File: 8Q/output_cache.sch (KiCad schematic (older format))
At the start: 21 parts

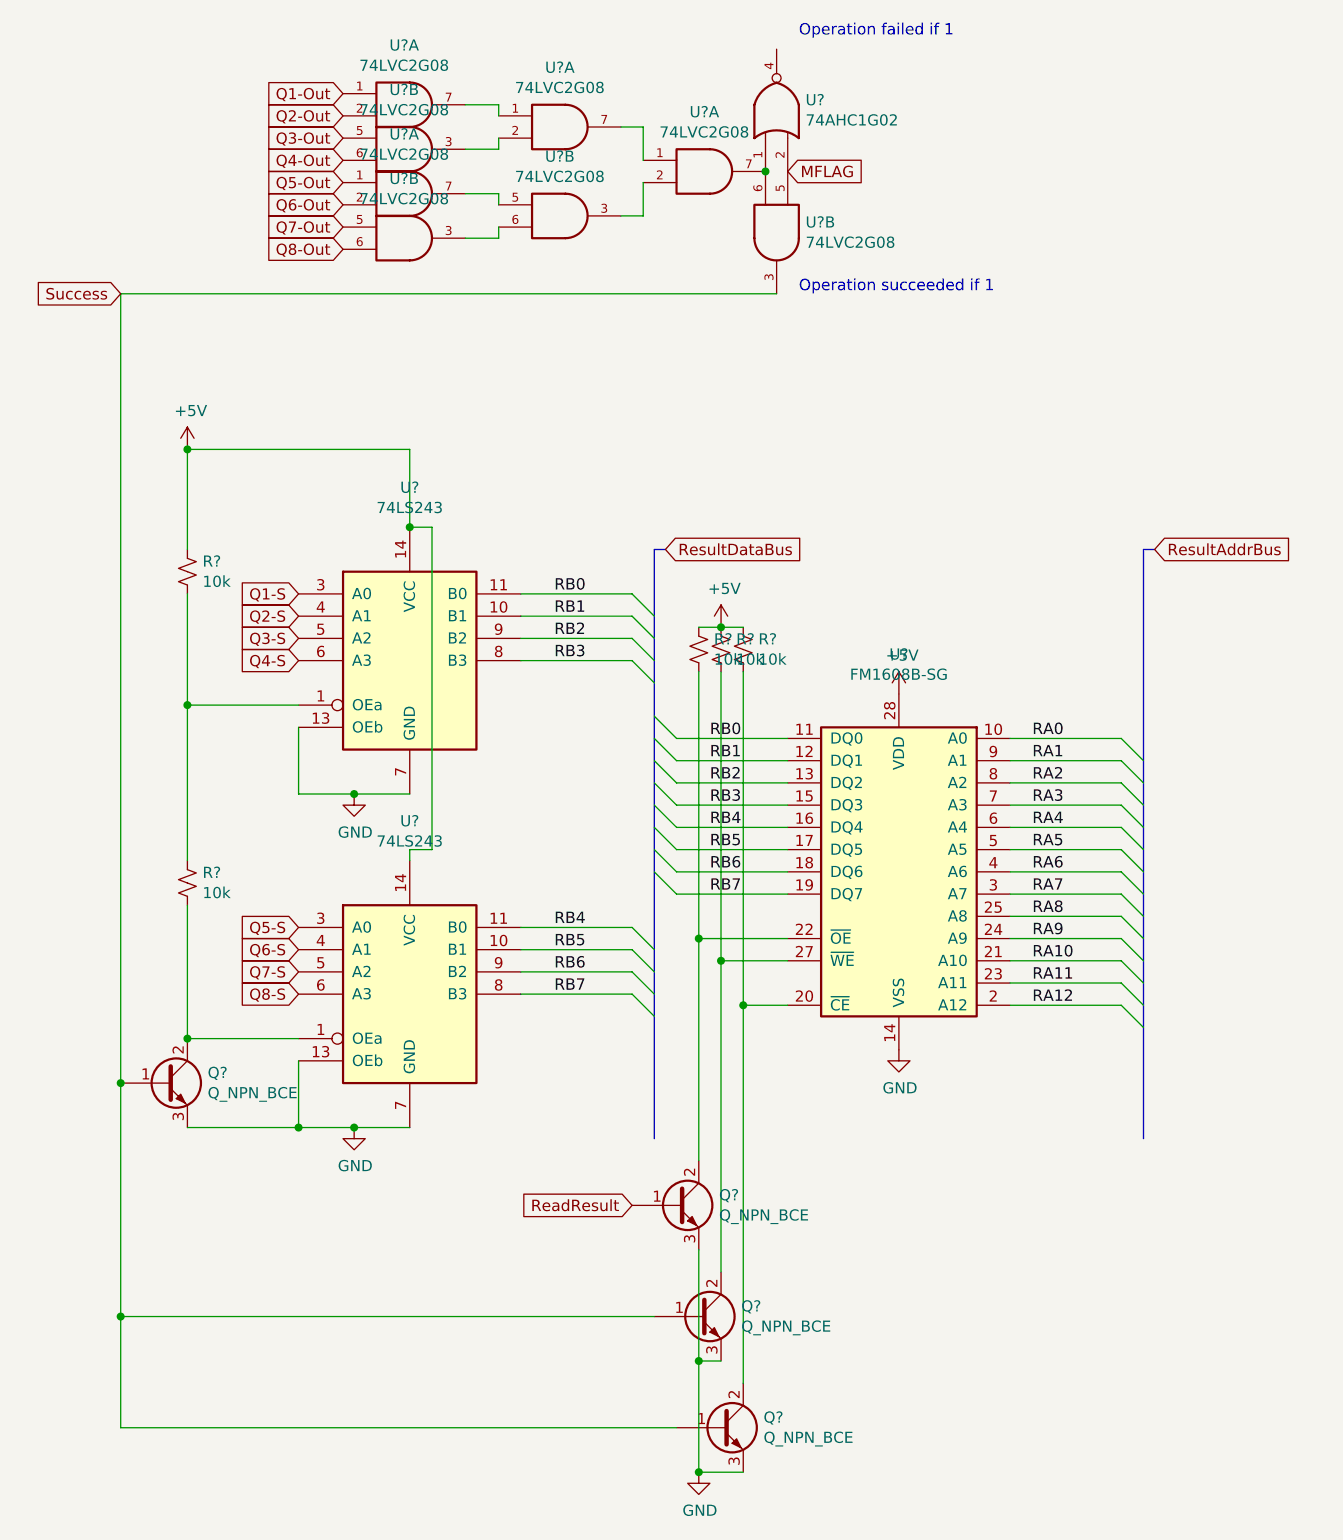
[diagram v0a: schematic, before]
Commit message: modified:   8Q/8Q-cache.lib 	new file:   8Q/8Q-rescue.dcm 	new file:   8Q/8Q-rescue.lib 	modified:   8Q/8Q.kicad_pcb 	modified:   8Q/8Q.sch 	modified:   8Q/8_qp_io.sch 	new file:   8Q/QGates.pretty/CH-Gate.kicad_mod 	new file:   8Q/QGates.pretty/CX-Gate.kicad_mod 	new file:   8Q/QGates.pretty/CY-Gate.kicad_mod 	new file:   8Q/QGates.pretty/CZ-Gate.kicad_mod 	new file:   8Q/QGates.pretty/H-Gate.kicad_mod 	new file:   8Q/QGates.pretty/Measure.kicad_mod 	new file:   8Q/QGates.pretty/Photon-Source.kicad_mod 	new file:   8Q/QGates.pretty/X-Gate.kicad_mod 	new file:   8Q/QGates.pretty/Y-Gate.kicad_mod 	new file:   8Q/QGates.pretty/Z-Gate.kicad_mod 	modified:   8Q/control_logic.sch 	modified:   8Q/cpu.sch 	modified:   8Q/inorder.sch 	modified:   8Q/instruction_bus.sch 	modified:   8Q/output_cache.sch 	modified:   8Q/power.sch 	modified:   8Q/preprocessor.sch 	modified:   8Q/qpower.sch 	modified:   8Q/qpu.sch 	new file:   8Q/sym-lib-table Introduced embedded QSeven module to replace CPU Computer now has support for: * 10Gbps Ethernet * 1xUSB3.0 * 4xUSB2.0 * 1xJTAG * 1xCAN * 1-Wire Bus * 1xSMBus * 1xI2C * External Watchdog * HDMI * LVDS
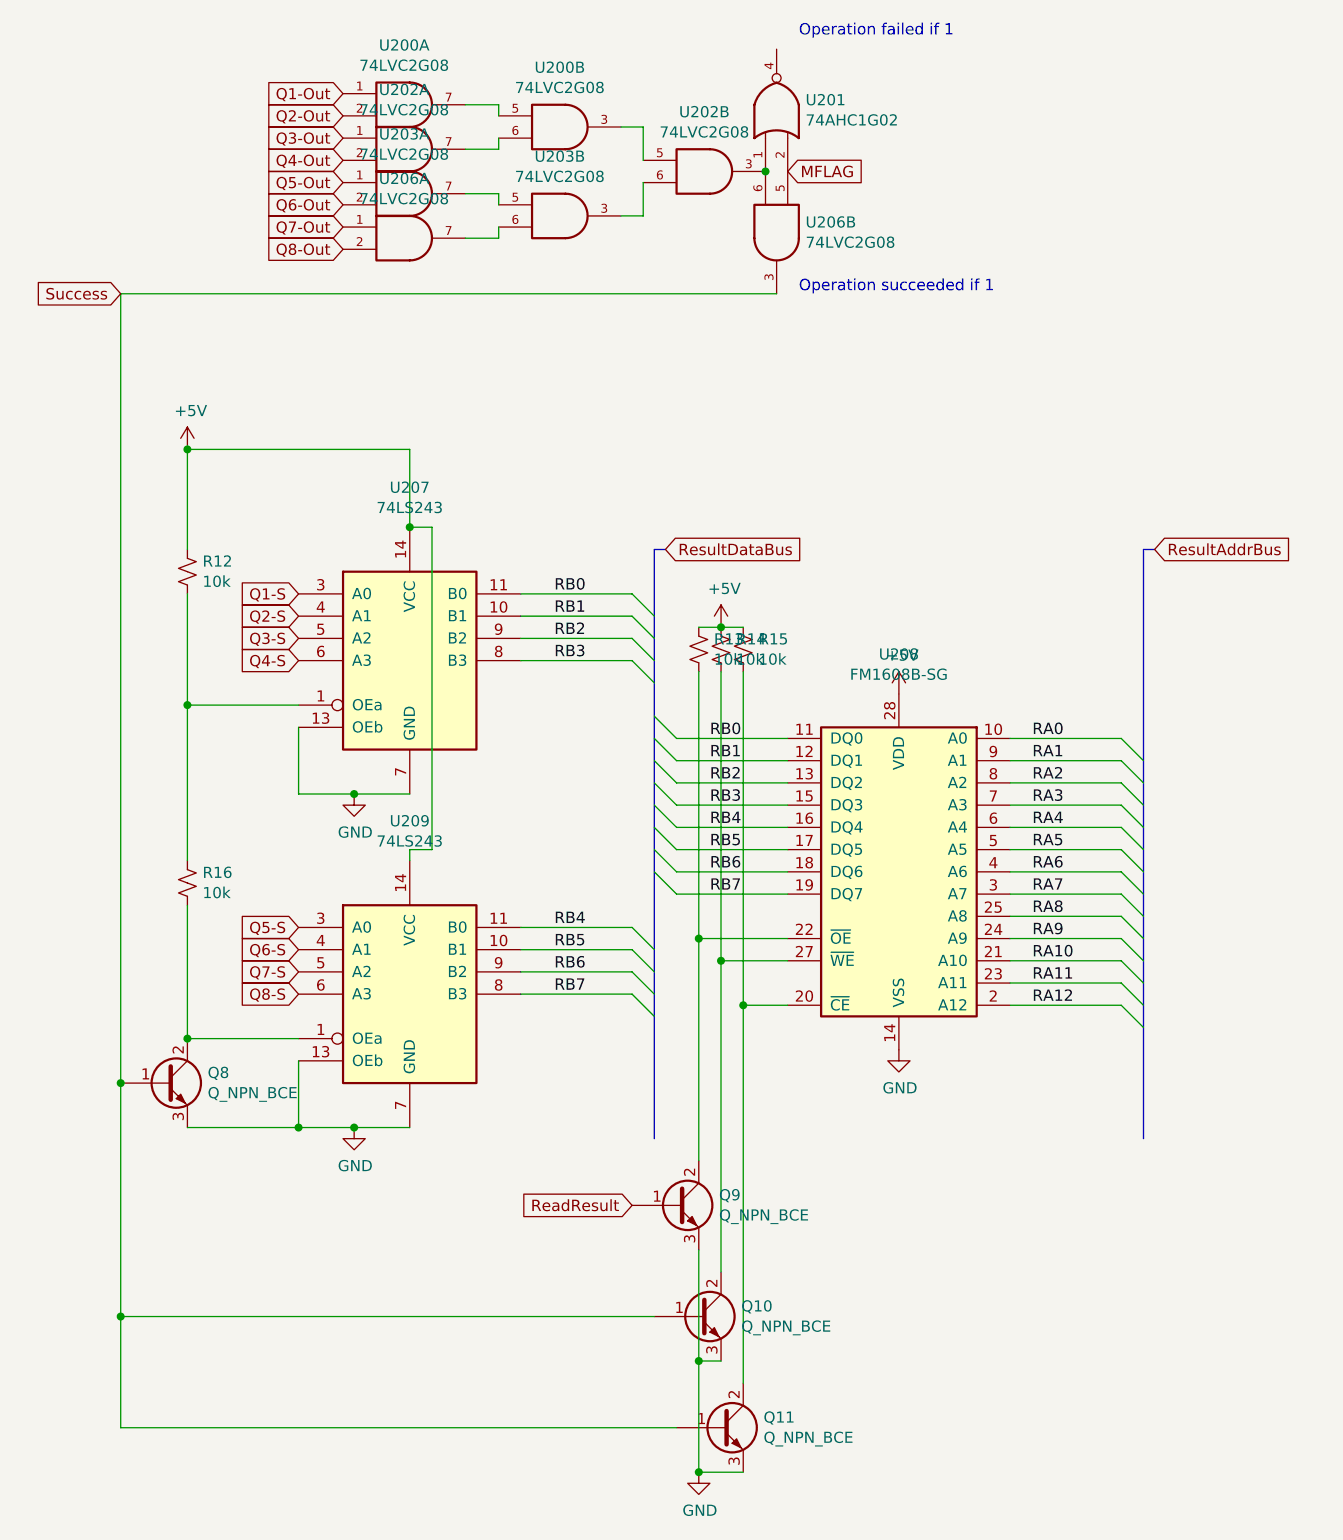
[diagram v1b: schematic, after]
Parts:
- gave numbers to parts that had none: 17
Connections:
- net Q3-Out: now also U202.1; no longer U202.5
- net Q4-Out: now also U202.2; no longer U202.6
- net Q7-Out: now also U206.1; no longer U206.5
- net Q8-Out: now also U206.2; no longer U206.6
- net at U200.7: now also U200.5; no longer U200.1
- net at U203.6: now also U206.7; no longer U206.3
- net at U203.3: now also U202.6; no longer U202.2
- net at U201.1, U206.6: now also U202.3; no longer U202.7
- new net: U200.6, U202.7
- new net: U200.3, U202.5
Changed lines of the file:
@@
 EESchema Schematic File Version 4
 LIBS:8Q-cache
+LIBS:Laptop-cache
 EELAYER 26 0
 EELAYER END
 $Descr A4 11693 8268
 encoding utf-8
-Sheet 12 13
+Sheet 12 11
 Title ""
 Date ""
@@
 Q8-S
 $Comp
-L 74xGxx:74LVC2G08 U?
+L 74xGxx:74LVC2G08 U200
 U 1 1 6E692EF1
 P 3700 1550
-F 0 "U?" H 3675 1817 50  0000 C CNN
+F 0 "U200" H 3675 1817 50  0000 C CNN
 F 1 "74LVC2G08" H 3675 1726 50  0000 C CNN
 F 2 "" H 3700 1550 50  0001 C CNN
@@
 $EndComp
 $Comp
-L 74xGxx:74LVC2G08 U?
-U 2 1 6E692F51
+L 74xGxx:74LVC2G08 U202
+U 1 1 6E692F51
 P 3700 1750
-F 0 "U?" H 3675 2017 50  0000 C CNN
+F 0 "U202" H 3675 2017 50  0000 C CNN
 F 1 "74LVC2G08" H 3675 1926 50  0000 C CNN
 F 2 "" H 3700 1750 50  0001 C CNN
 F 3 "http://www.ti.com/lit/sg/scyt129e/scyt129e.pdf" H 3700 1750 50  0001 C CNN
-	2    3700 1750
-	1    0    0    -1
-$EndComp
-$Comp
-L 74xGxx:74LVC2G08 U?
+	1    3700 1750
+	1    0    0    -1
+$EndComp
+$Comp
+L 74xGxx:74LVC2G08 U203
 U 1 1 6E692FB4
 P 3700 1950
-F 0 "U?" H 3675 2217 50  0000 C CNN
+F 0 "U203" H 3675 2217 50  0000 C CNN
 F 1 "74LVC2G08" H 3675 2126 50  0000 C CNN
 F 2 "" H 3700 1950 50  0001 C CNN
@@
 $EndComp
 $Comp
-L 74xGxx:74LVC2G08 U?
-U 2 1 6E693013
+L 74xGxx:74LVC2G08 U206
+U 1 1 6E693013
 P 3700 2150
-F 0 "U?" H 3675 2417 50  0000 C CNN
+F 0 "U206" H 3675 2417 50  0000 C CNN
 F 1 "74LVC2G08" H 3675 2326 50  0000 C CNN
 F 2 "" H 3700 2150 50  0001 C CNN
 F 3 "http://www.ti.com/lit/sg/scyt129e/scyt129e.pdf" H 3700 2150 50  0001 C CNN
-	2    3700 2150
-	1    0    0    -1
-$EndComp
-$Comp
-L 74xGxx:74LVC2G08 U?
-U 1 1 6E69303B
+	1    3700 2150
+	1    0    0    -1
+$EndComp
+$Comp
+L 74xGxx:74LVC2G08 U200
+U 2 1 6E69303B
 P 4400 1650
-F 0 "U?" H 4375 1917 50  0000 C CNN
+F 0 "U200" H 4375 1917 50  0000 C CNN
 F 1 "74LVC2G08" H 4375 1826 50  0000 C CNN
 F 2 "" H 4400 1650 50  0001 C CNN
 F 3 "http://www.ti.com/lit/sg/scyt129e/scyt129e.pdf" H 4400 1650 50  0001 C CNN
-	1    4400 1650
-	1    0    0    -1
-$EndComp
-$Comp
-L 74xGxx:74LVC2G08 U?
+	2    4400 1650
+	1    0    0    -1
+$EndComp
+$Comp
+L 74xGxx:74LVC2G08 U203
 U 2 1 6E69306B
 P 4400 2050
-F 0 "U?" H 4375 2317 50  0000 C CNN
+F 0 "U203" H 4375 2317 50  0000 C CNN
 F 1 "74LVC2G08" H 4375 2226 50  0000 C CNN
 F 2 "" H 4400 2050 50  0001 C CNN
@@
 $EndComp
 $Comp
-L 74xGxx:74LVC2G08 U?
-U 1 1 6E6930CF
+L 74xGxx:74LVC2G08 U202
+U 2 1 6E6930CF
 P 5050 1850
-F 0 "U?" H 5025 2117 50  0000 C CNN
+F 0 "U202" H 5025 2117 50  0000 C CNN
 F 1 "74LVC2G08" H 5025 2026 50  0000 C CNN
 F 2 "" H 5050 1850 50  0001 C CNN
 F 3 "http://www.ti.com/lit/sg/scyt129e/scyt129e.pdf" H 5050 1850 50  0001 C CNN
-	1    5050 1850
+	2    5050 1850
 	1    0    0    -1
 $EndComp
@@
 	4750 1650 4650 1650
 $Comp
-L 74xx:74LS243 U?
+L 74xx:74LS243 U207
 U 1 1 6E69629B
 P 3700 4050
-F 0 "U?" H 3700 4828 50  0000 C CNN
+F 0 "U207" H 3700 4828 50  0000 C CNN
 F 1 "74LS243" H 3700 4737 50  0000 C CNN
 F 2 "" H 3700 4050 50  0001 C CNN
@@
 $EndComp
 $Comp
-L 74xx:74LS243 U?
+L 74xx:74LS243 U209
 U 1 1 6E6963A5
 P 3700 5550
-F 0 "U?" H 3700 6328 50  0000 C CNN
+F 0 "U209" H 3700 6328 50  0000 C CNN
 F 1 "74LS243" H 3700 6237 50  0000 C CNN
 F 2 "" H 3700 5550 50  0001 C CNN
@@
 	3200 4650 3200 4350
 $Comp
-L 74xGxx:74LVC2G08 U?
+L 74xGxx:74LVC2G08 U206
 U 2 1 6E696CAD
 P 5350 2150
-F 0 "U?" V 5279 2280 50  0000 L CNN
+F 0 "U206" V 5279 2280 50  0000 L CNN
 F 1 "74LVC2G08" V 5370 2280 50  0000 L CNN
 F 2 "" H 5350 2150 50  0001 C CNN
@@
 MFLAG
 $Comp
-L 74xGxx:74AHC1G02 U?
+L 74xGxx:74AHC1G02 U201
 U 1 1 6E696ED6
 P 5350 1550
-F 0 "U?" V 5371 1420 50  0000 R CNN
+F 0 "U201" V 5371 1420 50  0000 R CNN
 F 1 "74AHC1G02" V 5280 1420 50  0000 R CNN
 F 2 "" H 5350 1550 50  0001 C CNN
@@
 Operation succeeded if 1
 $Comp
-L Memory_NVRAM:FM1608B-SG U?
+L Memory_NVRAM:FM1608B-SG U208
 U 1 1 6E69D7EB
 P 5900 5000
-F 0 "U?" H 5900 5978 50  0000 C CNN
+F 0 "U208" H 5900 5978 50  0000 C CNN
 F 1 "FM1608B-SG" H 5900 5887 50  0000 C CNN
 F 2 "Package_SO:SOIC-28W_7.5x17.9mm_P1.27mm" H 5900 5000 50  0001 C CNN
@@
 	6900 5600 7000 5700
 $Comp
-L power:+5V #PWR?
+L power:+5V #PWR0249
 U 1 1 6E6ABE73
 P 5900 4200
-F 0 "#PWR?" H 5900 4050 50  0001 C CNN
+F 0 "#PWR0249" H 5900 4050 50  0001 C CNN
 F 1 "+5V" H 5915 4373 50  0000 C CNN
 F 2 "" H 5900 4200 50  0001 C CNN
@@
 $EndComp
 $Comp
-L power:GND #PWR?
+L power:GND #PWR0251
 U 1 1 6E6ABEC0
 P 5900 5800
-F 0 "#PWR?" H 5900 5550 50  0001 C CNN
+F 0 "#PWR0251" H 5900 5550 50  0001 C CNN
 F 1 "GND" H 5905 5627 50  0000 C CNN
 F 2 "" H 5900 5800 50  0001 C CNN
@@
 $EndComp
 $Comp
-L power:GND #PWR?
+L power:GND #PWR0252
 U 1 1 6E6ABF06
 P 3450 6150
-F 0 "#PWR?" H 3450 5900 50  0001 C CNN
+F 0 "#PWR0252" H 3450 5900 50  0001 C CNN
 F 1 "GND" H 3455 5977 50  0000 C CNN
 F 2 "" H 3450 6150 50  0001 C CNN
@@
 $EndComp
 $Comp
-L power:GND #PWR?
+L power:GND #PWR0250
 U 1 1 6E6ABF4E
 P 3450 4650
-F 0 "#PWR?" H 3450 4400 50  0001 C CNN
+F 0 "#PWR0250" H 3450 4400 50  0001 C CNN
 F 1 "GND" H 3455 4477 50  0000 C CNN
 F 2 "" H 3450 4650 50  0001 C CNN
@@
 	2700 4250 3200 4250
 $Comp
-L Device:Q_NPN_BCE Q?
+L Device:Q_NPN_BCE Q8
 U 1 1 6E6ADCCF
 P 2600 5950
-F 0 "Q?" H 2791 5996 50  0000 L CNN
+F 0 "Q8" H 2791 5996 50  0000 L CNN
 F 1 "Q_NPN_BCE" H 2791 5905 50  0000 L CNN
 F 2 "" H 2800 6050 50  0001 C CNN
@@
 	2400 2400 5350 2400
 $Comp
-L power:+5V #PWR?
+L power:+5V #PWR0247
 U 1 1 6E6AFF81
 P 2700 3100
-F 0 "#PWR?" H 2700 2950 50  0001 C CNN
+F 0 "#PWR0247" H 2700 2950 50  0001 C CNN
 F 1 "+5V" H 2715 3273 50  0000 C CNN
 F 2 "" H 2700 3100 50  0001 C CNN
@@
 Connection ~ 2700 4250
 $Comp
-L Device:R_Small_US R?
+L Device:R_Small_US R12
 U 1 1 6E6B7BE8
 P 2700 3650
-F 0 "R?" H 2768 3696 50  0000 L CNN
+F 0 "R12" H 2768 3696 50  0000 L CNN
 F 1 "10k" H 2768 3605 50  0000 L CNN
 F 2 "" H 2700 3650 50  0001 C CNN
@@
 	2700 3750 2700 4250
 $Comp
-L Device:R_Small_US R?
+L Device:R_Small_US R16
 U 1 1 6E6B7C54
 P 2700 5050
-F 0 "R?" H 2768 5096 50  0000 L CNN
+F 0 "R16" H 2768 5096 50  0000 L CNN
 F 1 "10k" H 2768 5005 50  0000 L CNN
 F 2 "" H 2700 5050 50  0001 C CNN
@@
 Connection ~ 3200 6150
 $Comp
-L Device:Q_NPN_BCE Q?
+L Device:Q_NPN_BCE Q9
 U 1 1 6E6BC9A5
 P 4900 6500
-F 0 "Q?" H 5091 6546 50  0000 L CNN
+F 0 "Q9" H 5091 6546 50  0000 L CNN
 F 1 "Q_NPN_BCE" H 5091 6455 50  0000 L CNN
 F 2 "" H 5100 6600 50  0001 C CNN
@@
 ReadResult
 $Comp
-L Device:Q_NPN_BCE Q?
+L Device:Q_NPN_BCE Q10
 U 1 1 6E6C5C76
 P 5000 7000
-F 0 "Q?" H 5191 7046 50  0000 L CNN
+F 0 "Q10" H 5191 7046 50  0000 L CNN
 F 1 "Q_NPN_BCE" H 5191 6955 50  0000 L CNN
 F 2 "" H 5200 7100 50  0001 C CNN
@@
 $EndComp
 $Comp
-L Device:Q_NPN_BCE Q?
+L Device:Q_NPN_BCE Q11
 U 1 1 6E6C5CAA
 P 5100 7500
-F 0 "Q?" H 5291 7546 50  0000 L CNN
+F 0 "Q11" H 5291 7546 50  0000 L CNN
 F 1 "Q_NPN_BCE" H 5291 7455 50  0000 L CNN
 F 2 "" H 5300 7600 50  0001 C CNN
@@
 	5000 7200 5000 7700
 $Comp
-L power:GND #PWR?
+L power:GND #PWR0253
 U 1 1 6E6CD3BE
 P 5000 7700
-F 0 "#PWR?" H 5000 7450 50  0001 C CNN
+F 0 "#PWR0253" H 5000 7450 50  0001 C CNN
 F 1 "GND" H 5005 7527 50  0000 C CNN
 F 2 "" H 5000 7700 50  0001 C CNN
@@
 Connection ~ 5000 7700
 $Comp
-L Device:R_Small_US R?
+L Device:R_Small_US R13
 U 1 1 6E6D7495
 P 5000 4000
-F 0 "R?" H 5068 4046 50  0000 L CNN
+F 0 "R13" H 5068 4046 50  0000 L CNN
 F 1 "10k" H 5068 3955 50  0000 L CNN
 F 2 "" H 5000 4000 50  0001 C CNN
@@
 $EndComp
 $Comp
-L Device:R_Small_US R?
+L Device:R_Small_US R14
 U 1 1 6E6D750B
 P 5100 4000
-F 0 "R?" H 5168 4046 50  0000 L CNN
+F 0 "R14" H 5168 4046 50  0000 L CNN
 F 1 "10k" H 5168 3955 50  0000 L CNN
 F 2 "" H 5100 4000 50  0001 C CNN
@@
 $EndComp
 $Comp
-L Device:R_Small_US R?
+L Device:R_Small_US R15
 U 1 1 6E6D7543
 P 5200 4000
-F 0 "R?" H 5268 4046 50  0000 L CNN
+F 0 "R15" H 5268 4046 50  0000 L CNN
 F 1 "10k" H 5268 3955 50  0000 L CNN
 F 2 "" H 5200 4000 50  0001 C CNN
@@
 	5100 3900 5200 3900
 $Comp
-L power:+5V #PWR?
+L power:+5V #PWR0248
 U 1 1 6E6DAD99
 P 5100 3900
-F 0 "#PWR?" H 5100 3750 50  0001 C CNN
+F 0 "#PWR0248" H 5100 3750 50  0001 C CNN
 F 1 "+5V" H 5115 4073 50  0000 C CNN
 F 2 "" H 5100 3900 50  0001 C CNN
@@
 Wire Wire Line
 	2400 7500 2400 7000
+Connection ~ 2400 7000
+Text GLabel 2400 2400 0    51   Input ~ 0
+Success
 Wire Bus Line
 	7000 3550 7000 6200
 Wire Bus Line
 	4800 3550 4800 6200
-Connection ~ 2400 7000
-Text GLabel 2400 2400 0    51   Input ~ 0
-Success
 $EndSCHEMATC
